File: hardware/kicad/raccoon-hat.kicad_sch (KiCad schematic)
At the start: 41 parts, among them J1 GPIO, J2 HR911105A, J3 USB-A 3.0, T1 750342460, U1 SI3402-B, U2 TPS54302, U3 RTL8153B, U4 AP2112K-3.3, U5 W25Q16, Y1 25MHz

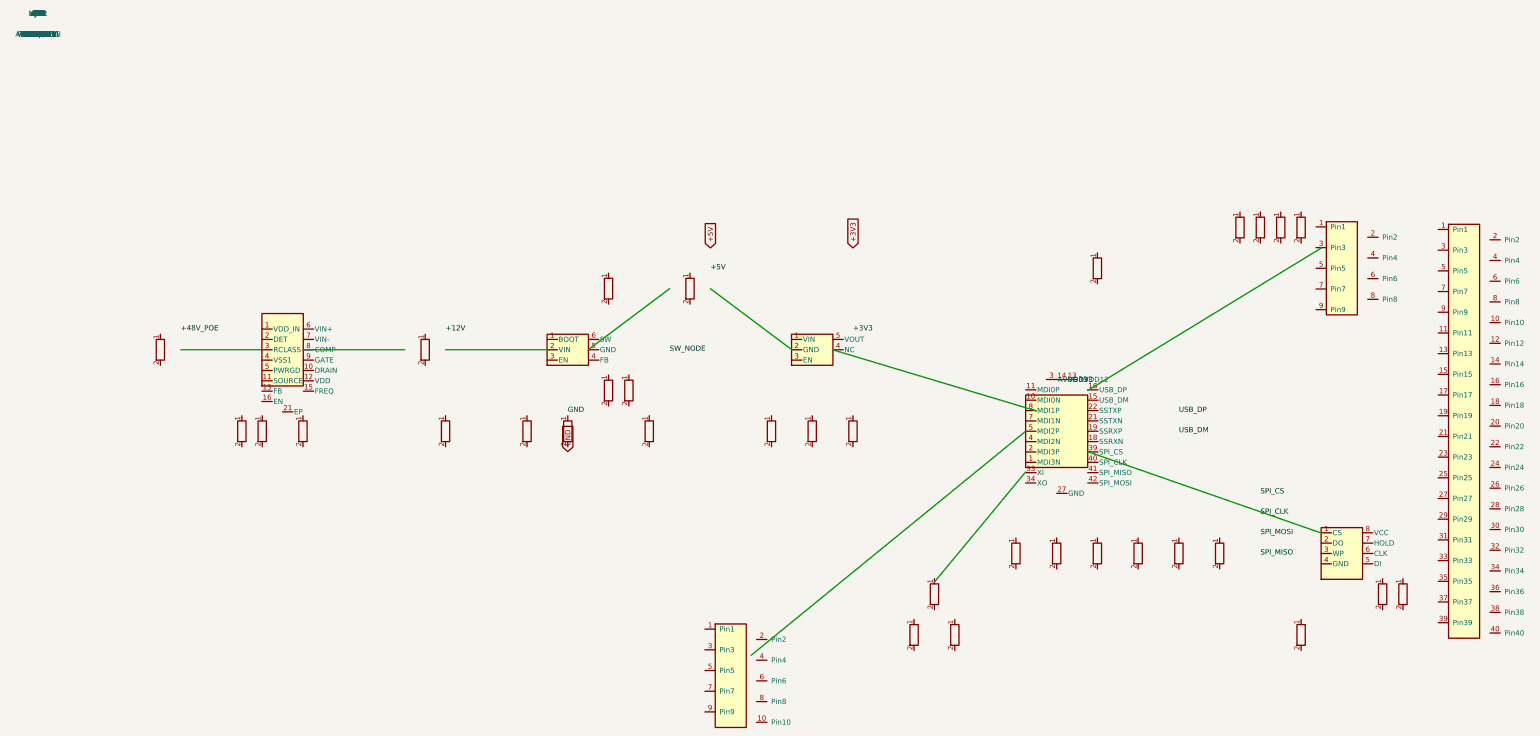
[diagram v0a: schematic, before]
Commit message: Added RDP/VNC
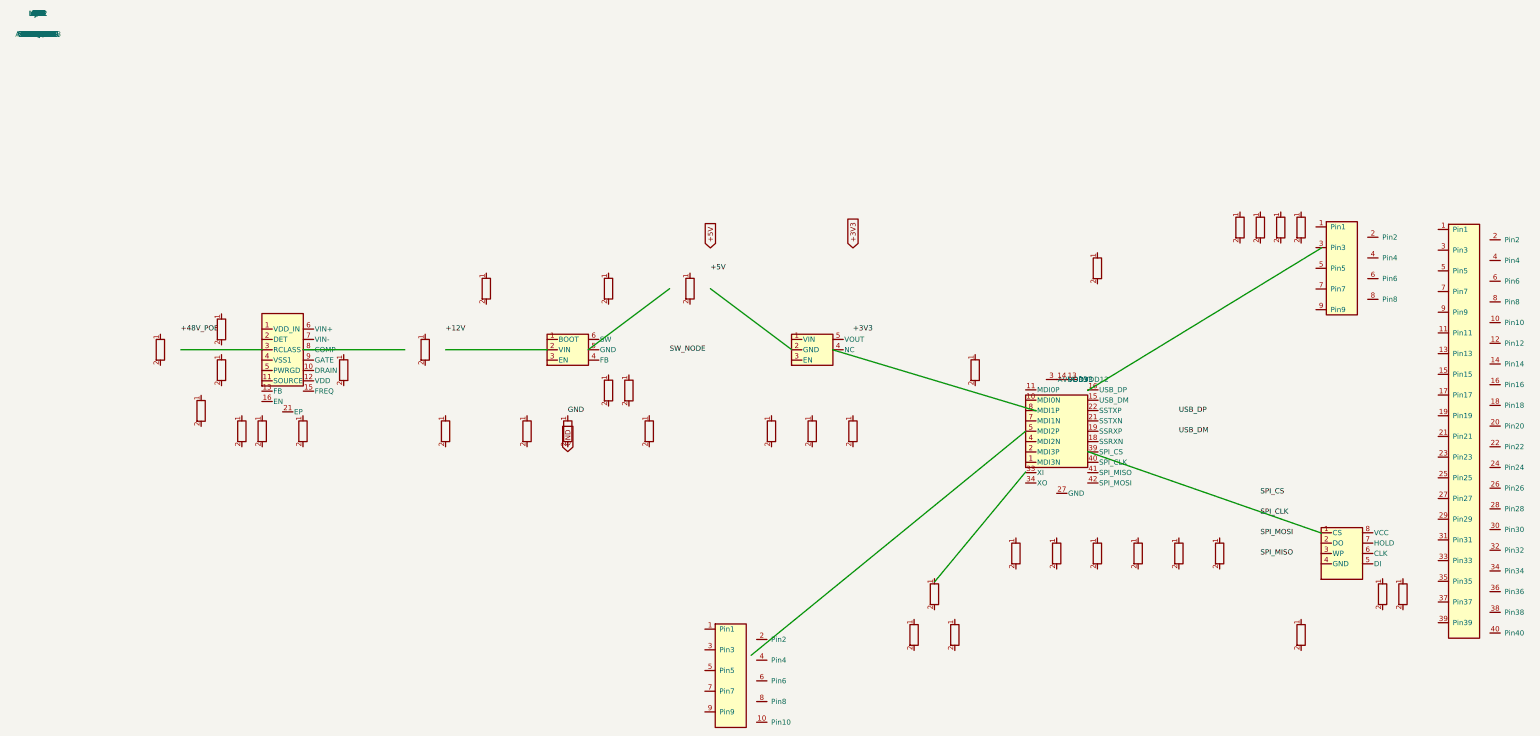
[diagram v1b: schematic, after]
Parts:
- added D1: MBRS340, Diode_SMD:D_SMA, symbol R
- added D2: SMBJ58A, Diode_SMD:D_SMA, symbol R
- added D3, D4: BAT54S, Package_TO_SOT_SMD:SOT-23, symbol R
- added L2: 4.7uH, Inductor_SMD:L_0805_2012Metric, symbol L
- added Q1: SI2302CDS, Package_TO_SOT_SMD:SOT-23, symbol R
- C13, C14: value 15pF -> 10pF
- R10: renamed from R2; value 5.36k -> 19.1K
- R9: renamed from R1; value 24.9k -> 100K
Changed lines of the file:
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@@
 	(symbol (lib_id "C") (at 215 150 0) (unit 1) (exclude_from_sim no) (in_bom yes) (on_board yes) (dnp no)
 		(property "Reference" "C13" (at 0 -2.54 0) (effects (font (size 1.27 1.27))))
-		(property "Value" "15pF" (at 0 2.54 0) (effects (font (size 1.27 1.27))))
+		(property "Value" "10pF" (at 0 2.54 0) (effects (font (size 1.27 1.27))))
 		(property "Footprint" "" (at 0 0 0) (effects (font (size 1.27 1.27)) hide))
 		(property "Datasheet" "" (at 0 0 0) (effects (font (size 1.27 1.27)) hide))
@@
 	(symbol (lib_id "C") (at 225 150 0) (unit 1) (exclude_from_sim no) (in_bom yes) (on_board yes) (dnp no)
 		(property "Reference" "C14" (at 0 -2.54 0) (effects (font (size 1.27 1.27))))
-		(property "Value" "15pF" (at 0 2.54 0) (effects (font (size 1.27 1.27))))
+		(property "Value" "10pF" (at 0 2.54 0) (effects (font (size 1.27 1.27))))
 		(property "Footprint" "" (at 0 0 0) (effects (font (size 1.27 1.27)) hide))
 		(property "Datasheet" "" (at 0 0 0) (effects (font (size 1.27 1.27)) hide))
@@
 	)
 	(symbol (lib_id "R") (at 140 90 0) (unit 1) (exclude_from_sim no) (in_bom yes) (on_board yes) (dnp no)
-		(property "Reference" "R1" (at 0 -2.54 0) (effects (font (size 1.27 1.27))))
-		(property "Value" "24.9k" (at 0 2.54 0) (effects (font (size 1.27 1.27))))
+		(property "Reference" "R9" (at 0 -2.54 0) (effects (font (size 1.27 1.27))))
+		(property "Value" "100K" (at 0 2.54 0) (effects (font (size 1.27 1.27))))
 		(property "Footprint" "" (at 0 0 0) (effects (font (size 1.27 1.27)) hide))
 		(property "Datasheet" "" (at 0 0 0) (effects (font (size 1.27 1.27)) hide))
 		(property "Description" "" (at 0 0 0) (effects (font (size 1.27 1.27)) hide))
-		(instances (project "raccoon-hat" (path "/578d96f6-37b6-428e-95b7-9f58a40b68ae" (reference "R1") (unit 1))))
+		(instances (project "raccoon-hat" (path "/578d96f6-37b6-428e-95b7-9f58a40b68ae" (reference "R9") (unit 1))))
 	)
 	(symbol (lib_id "R") (at 145 90 0) (unit 1) (exclude_from_sim no) (in_bom yes) (on_board yes) (dnp no)
-		(property "Reference" "R2" (at 0 -2.54 0) (effects (font (size 1.27 1.27))))
-		(property "Value" "5.36k" (at 0 2.54 0) (effects (font (size 1.27 1.27))))
+		(property "Reference" "R10" (at 0 -2.54 0) (effects (font (size 1.27 1.27))))
+		(property "Value" "19.1K" (at 0 2.54 0) (effects (font (size 1.27 1.27))))
 		(property "Footprint" "" (at 0 0 0) (effects (font (size 1.27 1.27)) hide))
 		(property "Datasheet" "" (at 0 0 0) (effects (font (size 1.27 1.27)) hide))
 		(property "Description" "" (at 0 0 0) (effects (font (size 1.27 1.27)) hide))
-		(instances (project "raccoon-hat" (path "/578d96f6-37b6-428e-95b7-9f58a40b68ae" (reference "R2") (unit 1))))
+		(instances (project "raccoon-hat" (path "/578d96f6-37b6-428e-95b7-9f58a40b68ae" (reference "R10") (unit 1))))
 	)
 	(symbol (lib_id "R") (at 295 50 0) (unit 1) (exclude_from_sim no) (in_bom yes) (on_board yes) (dnp no)
@@
 		(instances (project "raccoon-hat" (path "/578d96f6-37b6-428e-95b7-9f58a40b68ae" (reference "R8") (unit 1))))
 	)
+	(symbol (lib_id "R") (at 75 85 0) (unit 1) (exclude_from_sim no) (in_bom yes) (on_board yes) (dnp no)
+		(property "Reference" "Q1" (at 0 -2.54 0) (effects (font (size 1.27 1.27))))
+		(property "Value" "SI2302CDS" (at 0 2.54 0) (effects (font (size 1.27 1.27))))
+		(property "Footprint" "Package_TO_SOT_SMD:SOT-23" (at 0 0 0) (effects (font (size 1.27 1.27)) hide))
+		(property "Datasheet" "" (at 0 0 0) (effects (font (size 1.27 1.27)) hide))
+		(property "Description" "N-MOSFET inrush control (SI3402 GATE output)" (at 0 0 0) (effects (font (size 1.27 1.27)) hide))
+		(instances (project "raccoon-hat" (path "/578d96f6-37b6-428e-95b7-9f58a40b68ae" (reference "Q1") (unit 1))))
+	)
+	(symbol (lib_id "R") (at 110 65 0) (unit 1) (exclude_from_sim no) (in_bom yes) (on_board yes) (dnp no)
+		(property "Reference" "D1" (at 0 -2.54 0) (effects (font (size 1.27 1.27))))
+		(property "Value" "MBRS340" (at 0 2.54 0) (effects (font (size 1.27 1.27))))
+		(property "Footprint" "Diode_SMD:D_SMA" (at 0 0 0) (effects (font (size 1.27 1.27)) hide))
+		(property "Datasheet" "" (at 0 0 0) (effects (font (size 1.27 1.27)) hide))
+		(property "Description" "Schottky diode 40V 3A (flyback rectifier)" (at 0 0 0) (effects (font (size 1.27 1.27)) hide))
+		(instances (project "raccoon-hat" (path "/578d96f6-37b6-428e-95b7-9f58a40b68ae" (reference "D1") (unit 1))))
+	)
+	(symbol (lib_id "R") (at 40 95 0) (unit 1) (exclude_from_sim no) (in_bom yes) (on_board yes) (dnp no)
+		(property "Reference" "D2" (at 0 -2.54 0) (effects (font (size 1.27 1.27))))
+		(property "Value" "SMBJ58A" (at 0 2.54 0) (effects (font (size 1.27 1.27))))
+		(property "Footprint" "Diode_SMD:D_SMA" (at 0 0 0) (effects (font (size 1.27 1.27)) hide))
+		(property "Datasheet" "" (at 0 0 0) (effects (font (size 1.27 1.27)) hide))
+		(property "Description" "TVS diode 58V (PoE overvoltage protection)" (at 0 0 0) (effects (font (size 1.27 1.27)) hide))
+		(instances (project "raccoon-hat" (path "/578d96f6-37b6-428e-95b7-9f58a40b68ae" (reference "D2") (unit 1))))
+	)
+	(symbol (lib_id "R") (at 45 75 0) (unit 1) (exclude_from_sim no) (in_bom yes) (on_board yes) (dnp no)
+		(property "Reference" "D3" (at 0 -2.54 0) (effects (font (size 1.27 1.27))))
+		(property "Value" "BAT54S" (at 0 2.54 0) (effects (font (size 1.27 1.27))))
+		(property "Footprint" "Package_TO_SOT_SMD:SOT-23" (at 0 0 0) (effects (font (size 1.27 1.27)) hide))
+		(property "Datasheet" "" (at 0 0 0) (effects (font (size 1.27 1.27)) hide))
+		(property "Description" "Dual Schottky (PoE bridge VC2+ to VDD)" (at 0 0 0) (effects (font (size 1.27 1.27)) hide))
+		(instances (project "raccoon-hat" (path "/578d96f6-37b6-428e-95b7-9f58a40b68ae" (reference "D3") (unit 1))))
+	)
+	(symbol (lib_id "R") (at 45 85 0) (unit 1) (exclude_from_sim no) (in_bom yes) (on_board yes) (dnp no)
+		(property "Reference" "D4" (at 0 -2.54 0) (effects (font (size 1.27 1.27))))
+		(property "Value" "BAT54S" (at 0 2.54 0) (effects (font (size 1.27 1.27))))
+		(property "Footprint" "Package_TO_SOT_SMD:SOT-23" (at 0 0 0) (effects (font (size 1.27 1.27)) hide))
+		(property "Datasheet" "" (at 0 0 0) (effects (font (size 1.27 1.27)) hide))
+		(property "Description" "Dual Schottky (PoE bridge VC2- to VSS)" (at 0 0 0) (effects (font (size 1.27 1.27)) hide))
+		(instances (project "raccoon-hat" (path "/578d96f6-37b6-428e-95b7-9f58a40b68ae" (reference "D4") (unit 1))))
+	)
+	(symbol (lib_id "L") (at 230 85 0) (unit 1) (exclude_from_sim no) (in_bom yes) (on_board yes) (dnp no)
+		(property "Reference" "L2" (at 0 -2.54 0) (effects (font (size 1.27 1.27))))
+		(property "Value" "4.7uH" (at 0 2.54 0) (effects (font (size 1.27 1.27))))
+		(property "Footprint" "Inductor_SMD:L_0805_2012Metric" (at 0 0 0) (effects (font (size 1.27 1.27)) hide))
+		(property "Datasheet" "" (at 0 0 0) (effects (font (size 1.27 1.27)) hide))
+		(property "Description" "AVDD filter inductor for RTL8153B" (at 0 0 0) (effects (font (size 1.27 1.27)) hide))
+		(instances (project "raccoon-hat" (path "/578d96f6-37b6-428e-95b7-9f58a40b68ae" (reference "L2") (unit 1))))
+	)
 	(label "+48V_POE" (at 35 75 0) (effects (font (size 1.27 1.27))))

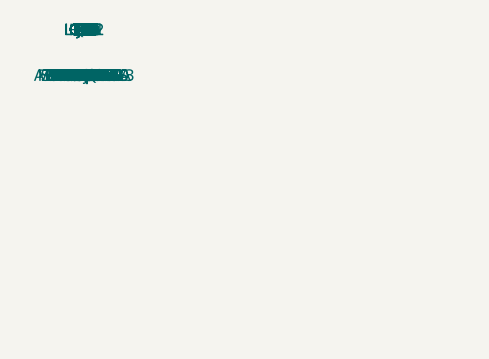
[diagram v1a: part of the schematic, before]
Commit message: Audit the v1 HAT hardware and fix the errors found
A structural audit of the KiCad sources and a datasheet review of the chosen
parts. The findings were severe enough that the v1 HAT is now documented as
concept stage rather than buildable. hardware/OPEN_QUESTIONS.md records every
finding with its source.

File state, established by parsing the files (KiCad was not available at the
time, so ERC/DRC could not be run):

  * raccoon-hat.kicad_pcb carried no net table at all and referenced nets by
    name where KiCad requires an integer index, in all 304 places. The file
    would not load. Repaired by tools/fix_pcb_nets.py: a 40-entry net table,
    integer ids on 228 pads and 73 segments, net_name on all 3 zones.
  * raccoon-hat.kicad_sch has effectively no connectivity: 47 symbols but 10
    wires, of which 19 of 20 endpoints land on empty canvas, 7 of 10 wires run
    diagonally, no junctions, no power symbols, and 15 labels none of which
    touch a wire. Netlist export would have been empty.
  * The PCB numbered its resistors R1-R8 where the guide and BOM used R3-R10;
    renumbered to match.

Electrical errors, each verified against the vendor datasheet:

  * R10 feedback divider: the guide assumed a 0.8V reference for the TPS54302
    and derived 19.1K. The real reference is 0.596V (SLVSDF3 6.3.7), so that
    divider yields 3.72V, not 5V, and a Pi 4 would not boot. Now 13.3K, the
    value TI tabulates for 5V. Telling detail: L1, C11+C12 and C1 all already
    matched TI's 5V row, so only the reference had been mis-transcribed.
  * R4 detection resistor was 25.5K, which is the value for the obsolete
    Si3402-A. Skyworks' migration note states it must be 24.3K for the -B.
  * R3 classification resistor was 49.9K. RCLASS is specified in ohms, not
    kilohms; 48.7R selects Class 3, which suits a ~12W PD.
  * R7/R8 LED series resistors were 10k, giving 0.13mA - effectively invisible.
    Now 1K.
  * The Si3402-B symbol matches no Si3402 variant: 0 of 16 pins ag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
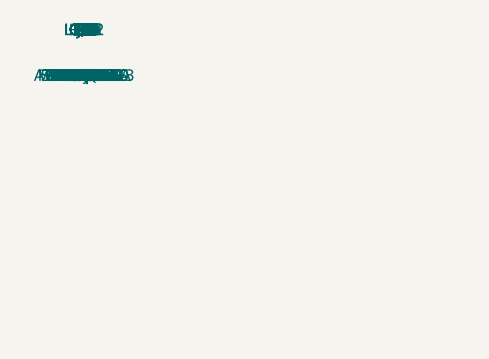
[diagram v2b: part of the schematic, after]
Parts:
- C8: value 10uF -> 100nF
- R10: value 19.1K -> 13.3K
- R3: value 330R -> 48.7R
- R4: value 330R -> 24.3K
- R5: value 25.5k -> 10K
- R7, R8: value 10k -> 1K
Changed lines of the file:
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@@
 	(symbol (lib_id "C") (at 200 100 0) (unit 1) (exclude_from_sim no) (in_bom yes) (on_board yes) (dnp no)
 		(property "Reference" "C8" (at 0 -2.54 0) (effects (font (size 1.27 1.27))))
-		(property "Value" "10uF" (at 0 2.54 0) (effects (font (size 1.27 1.27))))
+		(property "Value" "100nF" (at 0 2.54 0) (effects (font (size 1.27 1.27))))
 		(property "Footprint" "" (at 0 0 0) (effects (font (size 1.27 1.27)) hide))
 		(property "Datasheet" "" (at 0 0 0) (effects (font (size 1.27 1.27)) hide))
@@
 	(symbol (lib_id "R") (at 145 90 0) (unit 1) (exclude_from_sim no) (in_bom yes) (on_board yes) (dnp no)
 		(property "Reference" "R10" (at 0 -2.54 0) (effects (font (size 1.27 1.27))))
-		(property "Value" "19.1K" (at 0 2.54 0) (effects (font (size 1.27 1.27))))
+		(property "Value" "13.3K" (at 0 2.54 0) (effects (font (size 1.27 1.27))))
 		(property "Footprint" "" (at 0 0 0) (effects (font (size 1.27 1.27)) hide))
 		(property "Datasheet" "" (at 0 0 0) (effects (font (size 1.27 1.27)) hide))
@@
 	(symbol (lib_id "R") (at 295 50 0) (unit 1) (exclude_from_sim no) (in_bom yes) (on_board yes) (dnp no)
 		(property "Reference" "R3" (at 0 -2.54 0) (effects (font (size 1.27 1.27))))
-		(property "Value" "330R" (at 0 2.54 0) (effects (font (size 1.27 1.27))))
+		(property "Value" "48.7R" (at 0 2.54 0) (effects (font (size 1.27 1.27))))
 		(property "Footprint" "" (at 0 0 0) (effects (font (size 1.27 1.27)) hide))
 		(property "Datasheet" "" (at 0 0 0) (effects (font (size 1.27 1.27)) hide))
@@
 	(symbol (lib_id "R") (at 305 50 0) (unit 1) (exclude_from_sim no) (in_bom yes) (on_board yes) (dnp no)
 		(property "Reference" "R4" (at 0 -2.54 0) (effects (font (size 1.27 1.27))))
-		(property "Value" "330R" (at 0 2.54 0) (effects (font (size 1.27 1.27))))
+		(property "Value" "24.3K" (at 0 2.54 0) (effects (font (size 1.27 1.27))))
 		(property "Footprint" "" (at 0 0 0) (effects (font (size 1.27 1.27)) hide))
 		(property "Datasheet" "" (at 0 0 0) (effects (font (size 1.27 1.27)) hide))
@@
 	(symbol (lib_id "R") (at 65 100 0) (unit 1) (exclude_from_sim no) (in_bom yes) (on_board yes) (dnp no)
 		(property "Reference" "R5" (at 0 -2.54 0) (effects (font (size 1.27 1.27))))
-		(property "Value" "25.5k" (at 0 2.54 0) (effects (font (size 1.27 1.27))))
+		(property "Value" "10K" (at 0 2.54 0) (effects (font (size 1.27 1.27))))
 		(property "Footprint" "" (at 0 0 0) (effects (font (size 1.27 1.27)) hide))
 		(property "Datasheet" "" (at 0 0 0) (effects (font (size 1.27 1.27)) hide))
@@
 	(symbol (lib_id "R") (at 335 140 0) (unit 1) (exclude_from_sim no) (in_bom yes) (on_board yes) (dnp no)
 		(property "Reference" "R7" (at 0 -2.54 0) (effects (font (size 1.27 1.27))))
-		(property "Value" "10k" (at 0 2.54 0) (effects (font (size 1.27 1.27))))
+		(property "Value" "1K" (at 0 2.54 0) (effects (font (size 1.27 1.27))))
 		(property "Footprint" "" (at 0 0 0) (effects (font (size 1.27 1.27)) hide))
 		(property "Datasheet" "" (at 0 0 0) (effects (font (size 1.27 1.27)) hide))
@@
 	(symbol (lib_id "R") (at 260 60 0) (unit 1) (exclude_from_sim no) (in_bom yes) (on_board yes) (dnp no)
 		(property "Reference" "R8" (at 0 -2.54 0) (effects (font (size 1.27 1.27))))
-		(property "Value" "10k" (at 0 2.54 0) (effects (font (size 1.27 1.27))))
+		(property "Value" "1K" (at 0 2.54 0) (effects (font (size 1.27 1.27))))
 		(property "Footprint" "" (at 0 0 0) (effects (font (size 1.27 1.27)) hide))
 		(property "Datasheet" "" (at 0 0 0) (effects (font (size 1.27 1.27)) hide))
